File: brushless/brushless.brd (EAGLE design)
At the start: 30 x 48 mm, 71 parts, among them Q1 BUK7Y12-40E, Q2 BUK7Y12-40E, Q3 BUK7Y12-40E, Q4 BUK7Y12-40E, Q5 BUK7Y12-40E, Q6 BUK7Y12-40E, X2 MOTOR

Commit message: 0.25
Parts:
- UC1: device stm32:LQFP48 -> rhoban:STM32_LQFP48
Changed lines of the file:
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@@
 <attribute name="FARNELL" value="1581233" x="17.6578" y="2.5118" size="1.778" layer="27" display="off"/>
 </element>
-<element name="UC1" library="stm32" package="LQFP48" value="STM32F103CBT6" x="17.9182" y="12.951" rot="R180">
+<element name="UC1" library="rhoban" package="STM32_LQFP48" value="STM32F103CBT6" x="17.9182" y="12.951" rot="R180">
 <attribute name="FARNELL" value="1606327" x="17.9182" y="12.951" size="1.778" layer="27" rot="R180" display="off"/>
 </element>

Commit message: Fixing phase on bootstrap capcaitors
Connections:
- removed net N$11: C1.2, DRV1.6
- removed net N$14: C2.2, DRV2.6
- removed net N$18: C3.2, DRV3.6
- net U_PHASE: now also C1.2, DRV1.6
- net V_PHASE: now also C2.2, DRV2.6
- net W_PHASE: now also C3.2, DRV3.6
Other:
- board text added: "RHOBAN BLDC REV2"
- board text removed: "RHOBAN BLDC REV1"
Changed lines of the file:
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@@
 <wire x1="29.92" y1="46" x2="-0.08" y2="46" width="0" layer="20"/>
 <wire x1="-0.08" y1="46" x2="-0.08" y2="-1.968" width="0" layer="20"/>
-<text x="9.017" y="42.037" size="0.8128" layer="25">RHOBAN BLDC REV1</text>
+<text x="9.017" y="42.037" size="0.8128" layer="25">RHOBAN BLDC REV2</text>
 <text x="10.16" y="44.577" size="0.8128" layer="25">"MAY THE FORCE</text>
 <text x="12.192" y="43.561" size="0.8128" layer="25">BE WITH US"</text>
@@
 <wire x1="5.673" y1="8.3948" x2="16.1682" y2="17.201" width="0" layer="19" extent="1-16"/>
 </signal>
-<signal name="N$11">
-<contactref element="C1" pad="2"/>
-<contactref element="DRV1" pad="6"/>
-<wire x1="3.0568" y1="16.9942" x2="8.8226" y2="17.1798" width="0" layer="19" extent="16-16"/>
-</signal>
 <signal name="N$10">
 <contactref element="D2" pad="1"/>
@@
 <wire x1="12.658" y1="9.89" x2="12.9628" y2="11.857" width="0" layer="19" extent="16-16"/>
 </signal>
-<signal name="N$14">
-<contactref element="C2" pad="2"/>
-<contactref element="DRV2" pad="6"/>
-<wire x1="12.9628" y1="16.9434" x2="17.103" y2="17.1798" width="0" layer="19" extent="16-16"/>
-</signal>
 <signal name="N$15">
 <contactref element="D3" pad="1"/>
@@
 <contactref element="R12" pad="2"/>
 <wire x1="20.9892" y1="9.89" x2="21.548" y2="11.857" width="0" layer="19" extent="16-16"/>
-</signal>
-<signal name="N$18">
-<contactref element="C3" pad="2"/>
-<contactref element="DRV3" pad="6"/>
-<wire x1="21.548" y1="16.9434" x2="26.2978" y2="16.9004" width="0" layer="19" extent="16-16"/>
 </signal>
 <signal name="V_HIGH">
@@
 <wire x1="16.285" y1="26.48" x2="17.7" y2="26.48" width="2" layer="16"/>
 <wire x1="17.7" y1="26.48" x2="17.7" y2="30" width="2" layer="16"/>
+<contactref element="C3" pad="2"/>
+<contactref element="DRV3" pad="6"/>
 <wire x1="17.7" y1="34.2" x2="17.59" y2="34.895" width="0" layer="19" extent="16-16"/>
+<wire x1="21.548" y1="16.9434" x2="18.825" y2="26.48" width="0" layer="19" extent="16-16"/>
+<wire x1="26.2978" y1="16.9004" x2="21.548" y2="16.9434" width="0" layer="19" extent="16-16"/>
 </signal>
 <signal name="V_PHASE" class="2">
@@
 <wire x1="10" y1="33.625" x2="10" y2="30" width="2" layer="16"/>
 <wire x1="10" y1="30" x2="10" y2="26.48" width="2" layer="16"/>
+<contactref element="C2" pad="2"/>
+<contactref element="DRV2" pad="6"/>
+<wire x1="12.9628" y1="16.9434" x2="10.7" y2="26.48" width="0" layer="19" extent="16-16"/>
+<wire x1="17.103" y1="17.1798" x2="12.9628" y2="16.9434" width="0" layer="19" extent="16-16"/>
 </signal>
 <signal name="U_PHASE" class="2">
@@
 <wire x1="7.46" y1="30" x2="2.5" y2="30" width="2" layer="16"/>
 <wire x1="2.5" y1="30" x2="2.5" y2="27" width="2" layer="16"/>
-<wire x1="2.5" y1="27" x2="2.905" y2="26.48" width="0" layer="19" extent="1-16"/>
+<contactref element="C1" pad="2"/>
+<contactref element="DRV1" pad="6"/>
+<wire x1="2.5" y1="27" x2="2.435" y2="26.48" width="0" layer="19" extent="16-16"/>
+<wire x1="3.0568" y1="16.9942" x2="2.905" y2="26.48" width="0" layer="19" extent="16-16"/>
+<wire x1="8.8226" y1="17.1798" x2="3.0568" y2="16.9942" width="0" layer="19" extent="16-16"/>
 </signal>
 <signal name="HALLU">

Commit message: Updating designs
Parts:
- removed R13, R22, R26: 10K, SparkFun-Resistors:0805
- moved R36 2.48 mm to (15.4, 5.28)
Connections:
- net GND: no longer R13.1, R14.1, R17.1, R18.1, R22.1, R26.1
- net HALLU: no longer R26.2
- net HALLV: no longer R22.2
- net HALLW: no longer R13.2
- net N$1: now also R14.2
- net N$2: now also R17.2
- net N$7: now also R18.2
- net U_GATE_HIGH: no longer R14.2
- net U_PHASE: now also R14.1
- net V_GATE_HIGH: no longer R17.2
- net V_PHASE: now also R17.1
- net W_GATE_HIGH: no longer R18.2
- net W_PHASE: now also R18.1
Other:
- board text removed: ""MAY THE FORCE"
- board text removed: "--------------------------"
- board text removed: "BE WITH US""
- board text removed: "RHOBAN BLDC REV2"
- board text removed: "V+"

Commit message: 10 ohms on mos gates
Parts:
- R1, R2, R3, R4, R5, R6: value 1K -> 10
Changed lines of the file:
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@@
 <attribute name="FARNELL" value="2317446" x="8.7972" y="12.4952" size="1.778" layer="28" rot="MR180" display="off"/>
 </element>
-<element name="R1" library="SparkFun-Resistors" package="0805" value="1K" x="4.9878" y="35.5648" rot="R90">
+<element name="R1" library="SparkFun-Resistors" package="0805" value="10" x="4.9878" y="35.5648" rot="R90">
 <attribute name="PROD_ID" value=" " x="4.9878" y="35.5648" size="1.778" layer="27" rot="R90" display="off"/>
 <attribute name="VALUE" value=" " x="4.9878" y="35.5648" size="1.778" layer="27" rot="R90" display="off"/>
 <attribute name="FARNELL" value="2446904" x="4.9878" y="35.5648" size="1.778" layer="27" rot="R90" display="off"/>
 </element>
-<element name="R2" library="SparkFun-Resistors" package="0805" value="1K" x="4.9944" y="39.3652" rot="R270">
+<element name="R2" library="SparkFun-Resistors" package="0805" value="10" x="4.9944" y="39.3652" rot="R270">
 <attribute name="PROD_ID" value=" " x="4.9944" y="39.3652" size="1.778" layer="27" rot="R270" display="off"/>
 <attribute name="VALUE" value=" " x="4.9944" y="39.3652" size="1.778" layer="27" rot="R270" display="off"/>
 <attribute name="FARNELL" value="2446904" x="4.9944" y="39.3652" size="1.778" layer="27" rot="R270" display="off"/>
 </element>
-<element name="R3" library="SparkFun-Resistors" package="0805" value="1K" x="11.8204" y="35.4886" rot="R90">
+<element name="R3" library="SparkFun-Resistors" package="0805" value="10" x="11.8204" y="35.4886" rot="R90">
 <attribute name="PROD_ID" value=" " x="11.8204" y="35.4886" size="1.778" layer="27" rot="R90" display="off"/>
 <attribute name="VALUE" value=" " x="11.8204" y="35.4886" size="1.778" layer="27" rot="R90" display="off"/>
 <attribute name="FARNELL" value="2446904" x="11.8204" y="35.4886" size="1.778" layer="27" rot="R90" display="off"/>
 </element>
-<element name="R4" library="SparkFun-Resistors" package="0805" value="1K" x="11.6746" y="39.3652" rot="R270">
+<element name="R4" library="SparkFun-Resistors" package="0805" value="10" x="11.6746" y="39.3652" rot="R270">
 <attribute name="PROD_ID" value=" " x="11.6746" y="39.3652" size="1.778" layer="27" rot="R270" display="off"/>
 <attribute name="VALUE" value=" " x="11.6746" y="39.3652" size="1.778" layer="27" rot="R270" display="off"/>
 <attribute name="FARNELL" value="2446904" x="11.6746" y="39.3652" size="1.778" layer="27" rot="R270" display="off"/>
 </element>
-<element name="R5" library="SparkFun-Resistors" package="0805" value="1K" x="19.669" y="35.6918" rot="R90">
+<element name="R5" library="SparkFun-Resistors" package="0805" value="10" x="19.669" y="35.6918" rot="R90">
 <attribute name="PROD_ID" value=" " x="19.669" y="35.6918" size="1.778" layer="27" rot="R90" display="off"/>
 <attribute name="VALUE" value=" " x="19.669" y="35.6918" size="1.778" layer="27" rot="R90" display="off"/>
 <attribute name="FARNELL" value="2446904" x="19.669" y="35.6918" size="1.778" layer="27" rot="R90" display="off"/>
 </element>
-<element name="R6" library="SparkFun-Resistors" package="0805" value="1K" x="19.4216" y="39.3652" rot="R270">
+<element name="R6" library="SparkFun-Resistors" package="0805" value="10" x="19.4216" y="39.3652" rot="R270">
 <attribute name="PROD_ID" value=" " x="19.4216" y="39.3652" size="1.778" layer="27" rot="R270" display="off"/>
 <attribute name="VALUE" value=" " x="19.4216" y="39.3652" size="1.778" layer="27" rot="R270" display="off"/>

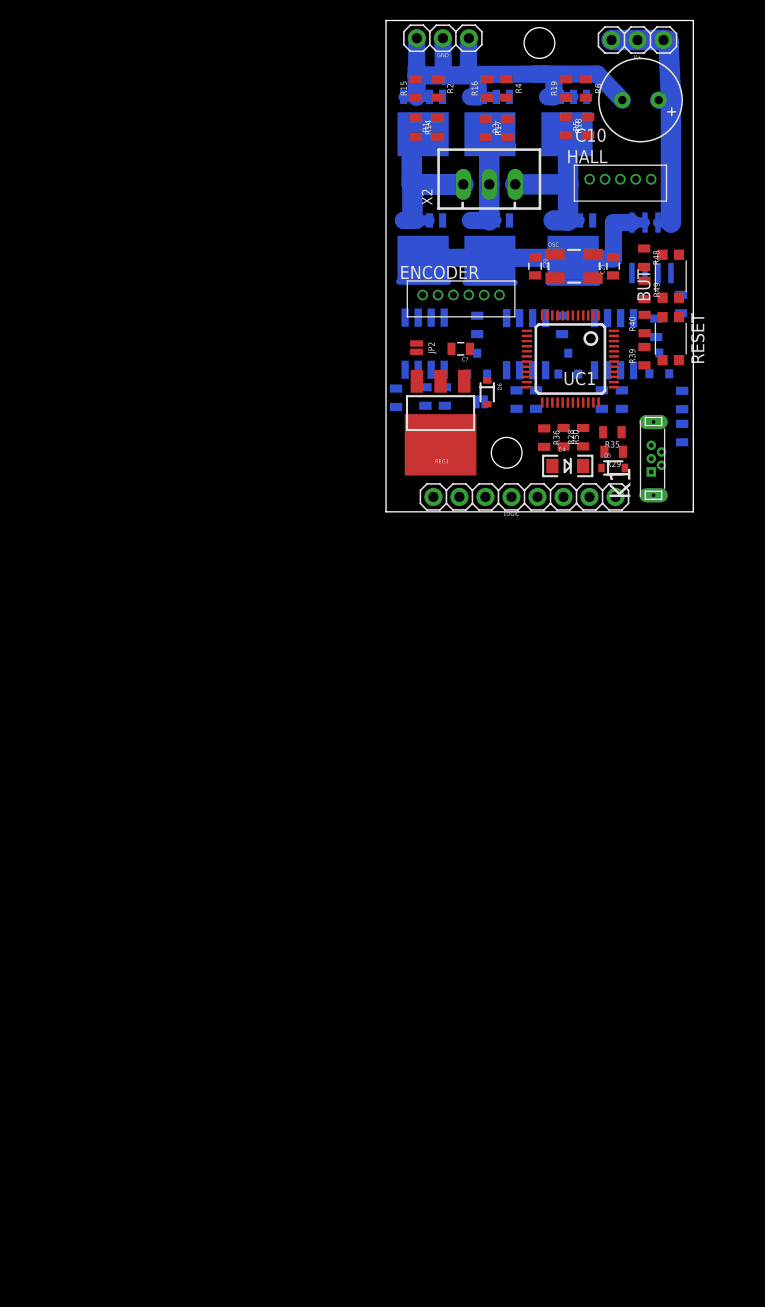
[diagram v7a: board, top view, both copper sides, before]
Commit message: schematic modified on brushless board
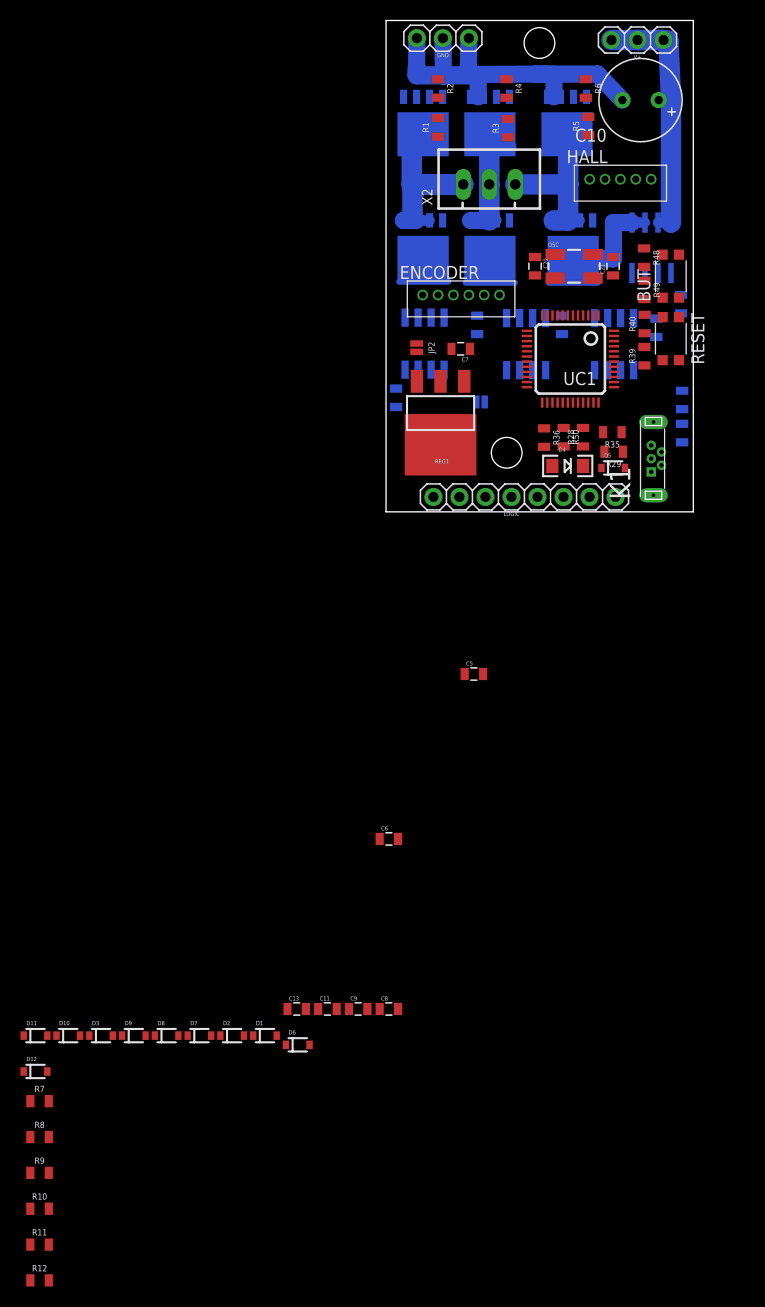
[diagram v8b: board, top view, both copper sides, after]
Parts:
- removed R14, R15, R16, R17, R18, R19: 10K, SparkFun-Resistors:0805
- added C11, C13, C9: 1000pF, SparkFun-Passives:0805@1
- added C5, C6, C8: 1uF, SparkFun-Passives:0805@1
- added D10, D11, D12, D7, D8, D9: (no value), SparkFun-DiscreteSemi:SOD-323
- D1, D2, D3: device rhoban:ZETEX_SOT-23 -> SparkFun-DiscreteSemi:SOD-323
- R10, R11, R12, R7, R8, R9: value 10K -> 10
- moved R12 102.0 mm to (-33.9, -77.0), flipped to the top, turned to 0 degrees
- moved R11 100.2 mm to (-33.9, -73.5), flipped to the top, turned to 0 degrees
- moved R10 91.7 mm to (-33.9, -70.0), flipped to the top, turned to 0 degrees
- moved R9 89.7 mm to (-33.9, -66.5), flipped to the top, turned to 0 degrees
- moved D3 85.3 mm to (-27.9, -53.1), flipped to the top, turned to 0 degrees
- moved R8 81.5 mm to (-33.9, -63.0), flipped to the top, turned to 0 degrees
- moved R7 79.4 mm to (-33.9, -59.5), flipped to the top, turned to 0 degrees
- moved D2 73.3 mm to (-15.1, -53.1), flipped to the top, turned to 0 degrees
- moved D1 68.8 mm to (-11.9, -53.1), flipped to the top, turned to 0 degrees
- moved D6 66.3 mm to (-8.70, -54.0), turned to 0 degrees
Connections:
- removed net 3.3: C12.2, C7.2, LOGIC.3, R40.1, R49.1, REG1.3, UC1.24, UC1.36, UC1.48, UC1.9
- removed net GND: C10.-, C12.1, C20.1, C21.1, C4.2, C7.1, D4.C, DRV1.4, DRV2.4, DRV3.4, ENCODER.1, GND.1, GND.2, GND.3, HALL.1, K1.5, K1.Z1, K1.Z2, LOGIC.1, Q2.1, Q2.2, Q2.3, Q4.1, Q4.2, Q4.3, Q6.1, Q6.2, Q6.3, R15.1, R16.1, R19.1, R21.2, R39.2, R48.2, R50.1, REG1.2, SENSE.5, UC1.23, UC1.35, UC1.47, UC1.8
- removed net N$1 (its old number): Q1.4, R1.2, R14.2
- removed net W_GATE_HIGH: DRV3.7, R5.1
- removed net W_GATE_LOW: DRV3.5, R19.2, R6.1
- new net +3V3: C11.1, C12.2, C7.2, LOGIC.3, R40.1, R49.1, REG1.3, UC1.24, UC1.36, UC1.48, UC1.9
- new net AGND: C10.-, C11.2, C12.1, C13.2, C20.1, C21.1, C4.2, C5.1, C6.1, C7.1, C8.1, C9.2, D4.C, DRV1.4, DRV2.4, DRV3.4, ENCODER.1, GND.1, GND.2, GND.3, HALL.1, K1.5, K1.Z1, K1.Z2, LOGIC.1, Q2.1, Q2.2, Q2.3, Q4.1, Q4.2, Q4.3, Q6.1, Q6.2, Q6.3, R21.2, R39.2, R48.2, R50.1, REG1.2, SENSE.5, UC1.23, UC1.35, UC1.47, UC1.8
- new net N$11: D1.2, Q1.4, R1.2
- new net N$12: D10.1, DRV3.7, R5.1
- new net N$13: D11.1, DRV3.5, R6.1
- new net VUSB1: D12.2
- net N$2: now also D7.2; no longer R17.2
- net N$22: now also C13.1, D12.1; no longer D6.1
- net N$3: now also D9.2
- net N$5: now also D6.1; no longer D1.1
- net N$6: now also D8.2
- net N$7: now also D10.2; no longer R18.2
- net N$9: now also D11.2
- net U_GATE_HIGH: now also D1.1
- net U_GATE_LOW: now also D9.1; no longer R15.2
- net U_PHASE: no longer R14.1
- net VCC: now also C9.1
- net VDRIVER: now also C5.2, C6.2, C8.2, D2.2, D3.2, D6.2; no longer D1.3, D2.3, D3.3
- net VUSB: no longer D6.2
- net V_GATE_HIGH: now also D7.1
- net V_GATE_LOW: now also D8.1; no longer R16.2
- net V_PHASE: no longer R17.1
- net W_PHASE: no longer R18.1
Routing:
- net GND: track 49.4 -> 0.00 mm
- net AGND: track 0.00 -> 38.3 mm
- net V+_MOS: track 25.3 -> 10.6 mm
- net V+: track 25.9 -> 24.9 mm
